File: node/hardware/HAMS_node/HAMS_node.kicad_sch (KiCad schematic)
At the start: 45 parts, among them J1 Conn_01x02, J2 Conn_02x07_Odd_Even, J3 Conn_01x08, J4 Conn_01x04, J5 Conn_01x04, J6 Conn_01x04, J7 Conn_01x04, Q1 DMP3099L, SW1 TL3305BF100QG, SW2 JS202011SCQN, U1 NRF24L01_Breakout, U2 nRF24L01p SMD module, U3 STM32L031K6Tx, Y1 CM9V-T1A

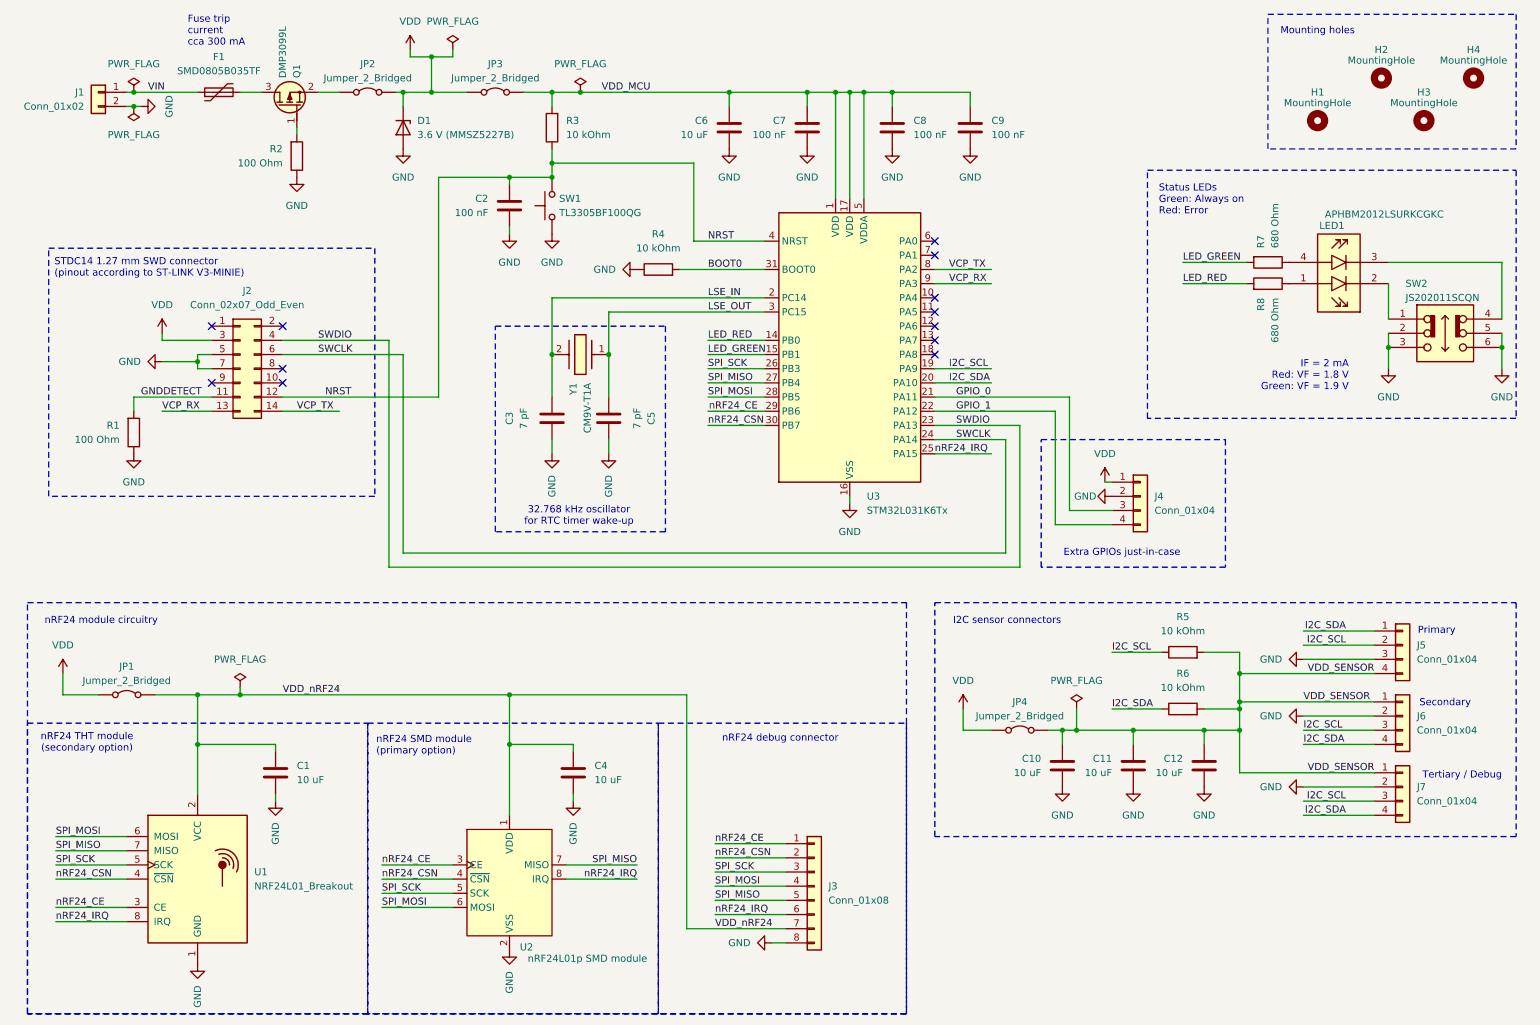
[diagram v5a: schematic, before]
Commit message: Improve HAMS hub HW: status button rework
Replace toggle switch with tactile switch for status button.
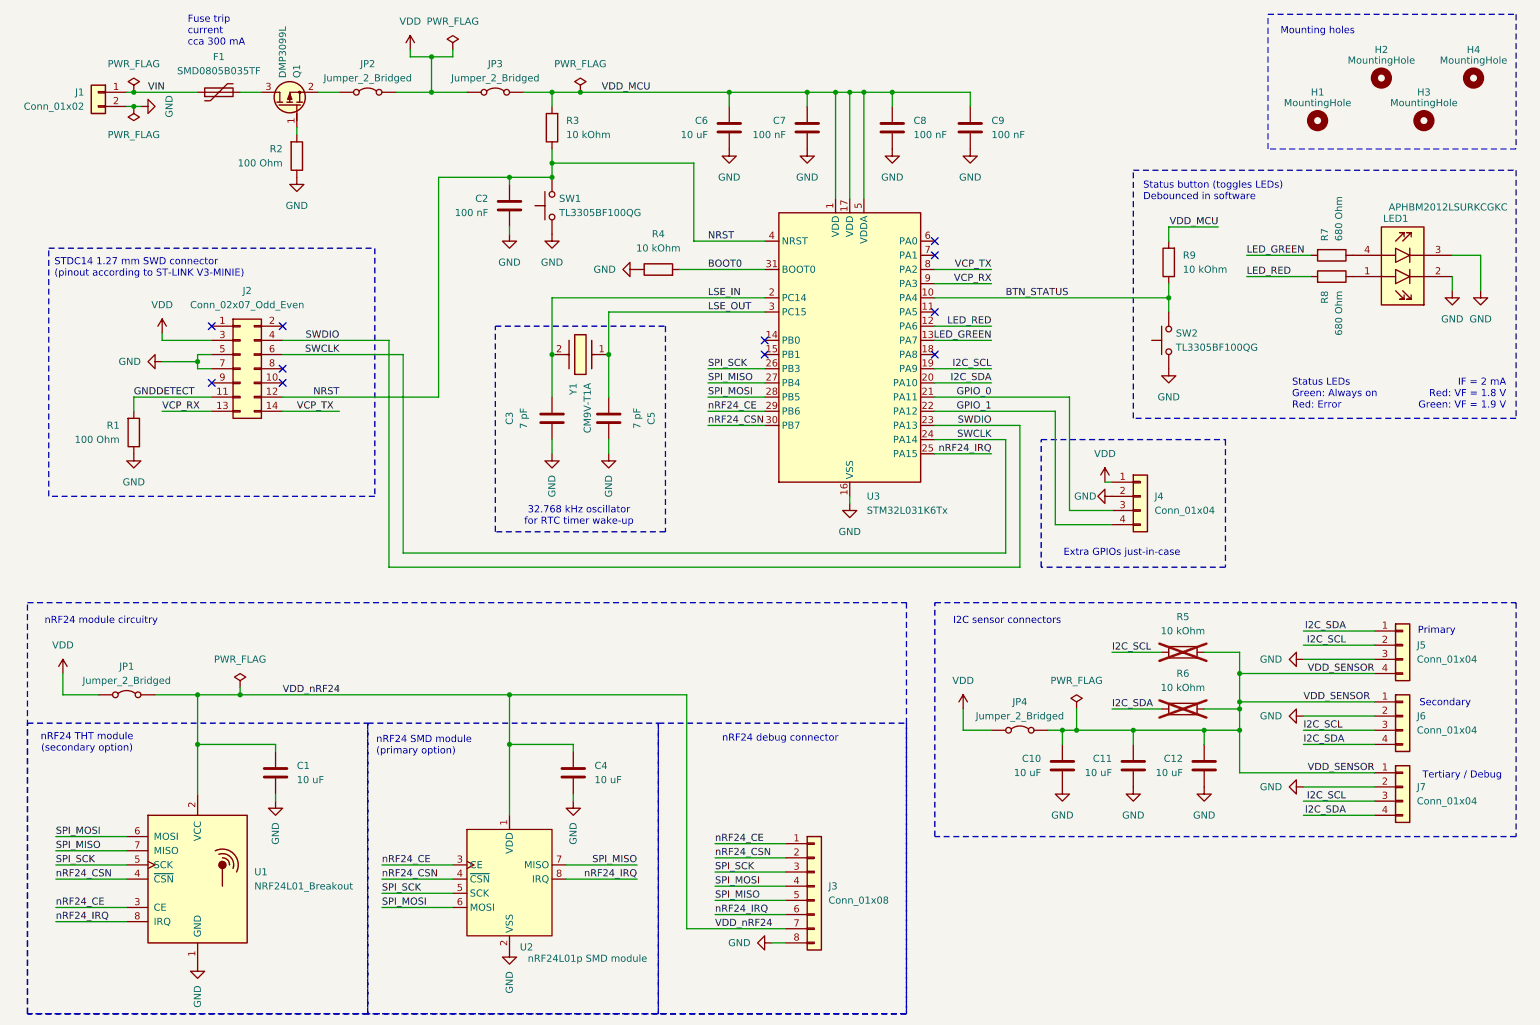
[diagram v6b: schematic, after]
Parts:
- removed D1: 3.6 V (MMSZ5227B), PCM_Diode_SMD_Handsoldering_AKL:D_SOD-123_Zener, symbol Device:D_Zener
- removed SW2: JS202011SCQN, Personal_SamacSys:JS202011SCQN, symbol Personal_SamacSys:JS202011SCQN
- added R9: 10 kOhm, Resistor_SMD:R_0603_1608Metric_Pad0.98x0.95mm_HandSolder, symbol Device:R
- added SW2: TL3305BF100QG, Personal_Switches:E-Switch_TL3305BF100QG_Tactile_SPST, symbol Switch:SW_Push
- JP1, JP2, JP3, JP4: footprint Connector_PinHeader_1.27mm:PinHeader_2x01_P1.27mm_Vertical -> Connector_PinHeader_1.27mm:PinHeader_1x02_P1.27mm_Vertical
- R5, R6: now not fitted
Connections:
- net GND: now also LED1.2 (CATHODE_RED), LED1.3 (CATHODE_GREEN), SW2.1
- net LED_GREEN: now also U3.13 (PA7); no longer U3.15 (PB1)
- net LED_RED: now also U3.12 (PA6); no longer U3.14 (PB0)
- net VDD_MCU: now also R9.2
- net BTN_STATUS: now reaches U3.10 (PA4)
- net BTN_STATUS: now also R9.1, SW2.2
- no-connect marks 12 -> 11
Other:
- note added: "Status button (toggles LEDs) Debounced in software"
- moved on the sheet: LED1, R7, R8
